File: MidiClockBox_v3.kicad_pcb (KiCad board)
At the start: 2 copper layers, 219 x 100 mm, 85 parts, among them J1 Midi In 0, J10 Display, J11 Midi Out 3, J12 Midi Out 4, J13 Midi Out 5, J14 Sync Out 0, J15 Sync Out 1, J16 Spare, J2 ICSP, J3 WS2812, J4 Conn_02x07_Odd_Even, J5 Conn_02x12_Counter_Clockwise, J6 Midi Out 0, J7 Midi Out 1, J8 Midi Out 2, J9 WS2812, SW1 RotaryEncoder_Switch, SW2 TAP, SW3 Start, SW4 Stop, SW5 Preset1, SW6 Preset2, SW7 Preset3, U1 CD74HC4067SM, U2 74LS241, U3 6N138, U4 74HC595, U6 74LS08, U7 74LS08, U8 74HC595, U9 74LS241

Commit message: add recent changes
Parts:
- added REF**: PinHeader_1x07_P2.54mm_Vertical, Connector_PinHeader_2.54mm:PinHeader_1x07_P2.54mm_Vertical, F.Cu at (164.4, 75.5)
- added REF**: PinHeader_1x07_P2.54mm_Vertical, Connector_PinHeader_2.54mm:PinHeader_1x07_P2.54mm_Vertical, F.Cu at (166.5, 83.5)
- moved J4 63.7 mm to (97.7, 116.5), turned to -90 degrees
- moved R15 56.8 mm to (127.0, 88.8), turned to -90 degrees
- moved C4 40.5 mm to (215.7, 64.8)
- moved U8 40.5 mm to (213.0, 71.5)
- moved C3 37.9 mm to (226.6, 53.6)
- moved U4 37.9 mm to (224.0, 60.0)
- moved R11 37.9 mm to (120.0, 88.8), turned to -90 degrees
- moved C2 31.6 mm to (202.6, 43.8)
- moved U2 31.6 mm to (206.0, 52.0)
- moved R9 31.0 mm to (116.0, 88.7), turned to -90 degrees
- moved J16 29.5 mm to (242.9, 74.5), turned to -90 degrees
- moved C7 27.0 mm to (242.6, 49.8), turned to 0 degrees
- moved R8 25.3 mm to (113.0, 88.7)
- moved R1 21.0 mm to (123.5, 88.7), turned to -90 degrees
- moved R7 19.7 mm to (110.0, 88.7)
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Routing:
- net IN_TAP: track 0.00 -> 265.2 mm, vias 0 -> 1
- net IN_START: track 0.00 -> 162.8 mm
- net SYNC_START_STOP_BUFFERED_0: track 0.00 -> 159.1 mm, vias 0 -> 4
- net SYNC_START_STOP_BUFFERED_1: track 0.00 -> 149.1 mm, vias 0 -> 4
- net DA1: track 0.00 -> 118.2 mm, vias 0 -> 4
- net MIDI_RX: track 0.00 -> 112.9 mm, vias 0 -> 4
- net DA0: track 0.00 -> 108.1 mm, vias 0 -> 2
- net IN_PRESET1: track 0.00 -> 107.2 mm
- net DA2: track 0.00 -> 104.5 mm, vias 0 -> 4
- net MIDI_TX: track 0.00 -> 102.8 mm, vias 0 -> 9
- net SYNC_TX_BUFFERED_1: track 0.00 -> 94.8 mm, vias 0 -> 6
- net IN_PRESET2: track 0.00 -> 92.9 mm
- net ENC_SW: track 0.00 -> 92.8 mm
- net SYNC_TX_BUFFERED_0: track 0.00 -> 91.8 mm, vias 0 -> 6
- net IN_15: track 0.00 -> 90.9 mm, vias 0 -> 2
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- added copper zone on B.Cu, net GND
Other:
- outline, holes or cut-outs redrawn
- board text removed: "Ports auf single board incl Arduino LED Stripe einzeln Buttons auf single board, wenig zuleitung, 2-seitig Panelize"

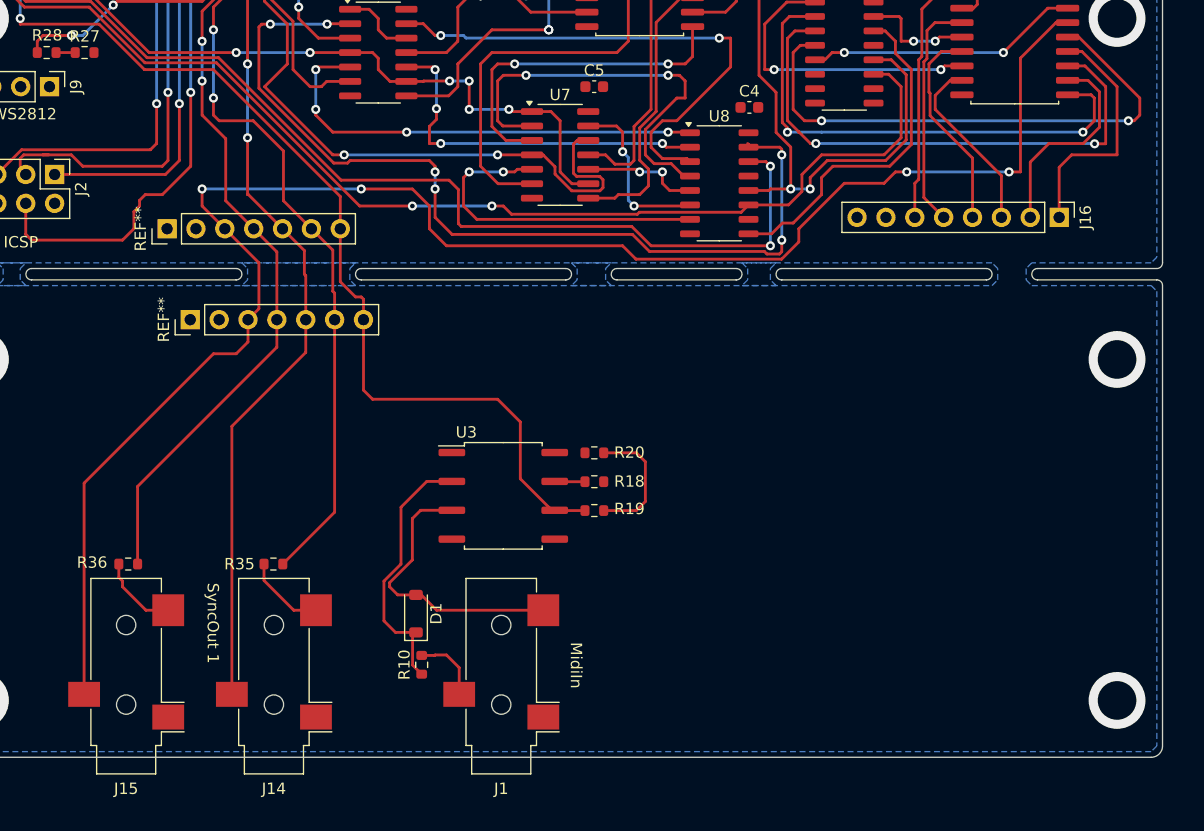
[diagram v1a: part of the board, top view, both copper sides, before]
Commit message: add breakout connectors for sync-out and midi-in
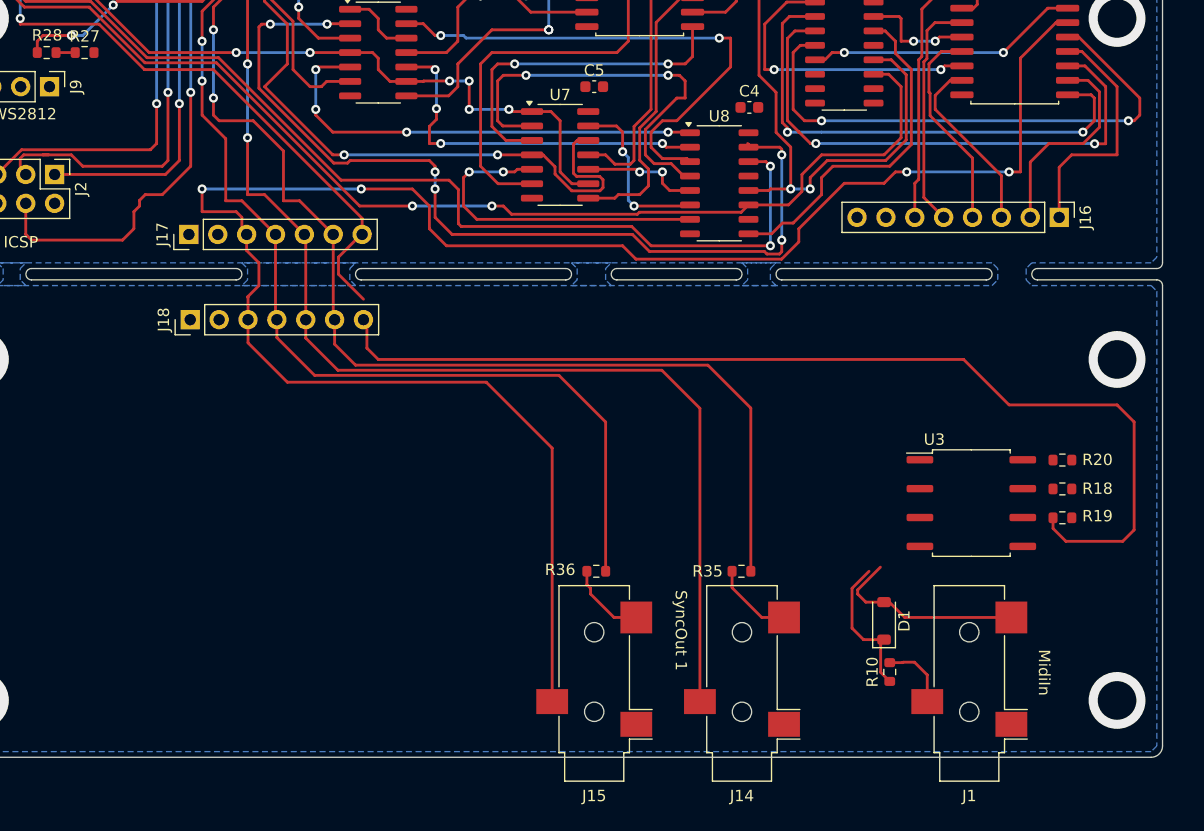
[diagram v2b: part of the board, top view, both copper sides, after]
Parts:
- removed REF** (x2): PinHeader_1x07_P2.54mm_Vertical, Connector_PinHeader_2.54mm:PinHeader_1x07_P2.54mm_Vertical
- added J17: Conn_01x07, Connector_PinHeader_2.54mm:PinHeader_1x07_P2.54mm_Vertical, F.Cu at (166.3, 76.0)
- added J18: Conn_01x07, Connector_PinHeader_2.54mm:PinHeader_1x07_P2.54mm_Vertical, F.Cu at (166.5, 83.5)
- moved D1 41.2 mm to (227.5, 110.0)
- moved J1 41.2 mm to (235.0, 115.5)
- moved J14 41.2 mm to (215.0, 115.5)
- moved J15 41.2 mm to (202.0, 115.5)
- moved R10 41.2 mm to (228.0, 114.5)
- moved R18 41.2 mm to (243.2, 98.4)
- moved R19 41.2 mm to (243.2, 100.9)
- moved R20 41.2 mm to (243.2, 95.9)
- moved R35 41.2 mm to (215.0, 105.6)
- moved R36 41.2 mm to (202.2, 105.6)
- moved U3 41.2 mm to (235.2, 99.6)
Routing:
- net MIDI_RX: track 112.9 -> 170.6 mm
- net SYNC_TX_BUFFERED_0: track 91.8 -> 124.7 mm
- net SYNC_START_STOP_BUFFERED_0: track 159.1 -> 188.9 mm
- net SYNC_TX_BUFFERED_1: track 94.8 -> 115.8 mm
- net SYNC_START_STOP_BUFFERED_1: track 149.1 -> 165.7 mm
- net Net-(R19-Pad2): track 11.5 -> 0.00 mm
- net Net-(D1-K): track 23.4 -> 13.0 mm
- net Net-(D1-A): track 25.0 -> 17.6 mm
- net Net-(U3-VO1): track 2.67 -> 0.00 mm

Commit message: pcb looks complete
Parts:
- added J19: Conn_02x05_Odd_Even, Connector_PinHeader_2.54mm:PinHeader_2x05_P2.54mm_Vertical, F.Cu at (155.2, 64.9)
- added J20: Conn_02x05_Odd_Even, Connector_PinHeader_2.54mm:PinHeader_2x05_P2.54mm_Vertical, F.Cu at (44.2, 64.9)
- moved J9 112.1 mm to (44.4, 39.5), turned to 90 degrees
- moved J2 98.3 mm to (246.5, 35.9), turned to 0 degrees
- moved R28 14.5 mm to (165.5, 68.7), turned to -90 degrees
- moved R27 9.90 mm to (165.5, 65.3), turned to 90 degrees
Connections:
- D2 pad 4: Net-(D2-DIN) -> LED_DATA
- J3 pad 2: Net-(D2-DIN) -> LED_DATA
- J5 pad 13: LED_DATA -> Net-(J5-Pin_13)
- J9 pad 2: Net-(J9-Pin_2) -> LED_DATA
- R27 pad 2: Net-(J9-Pin_2) -> Net-(J5-Pin_13)
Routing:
- net S0: track 0.08 -> 169.3 mm, vias 0 -> 8
- net S1: track 0.00 -> 166.7 mm, vias 0 -> 6
- net GND: track 0.00 -> 159.4 mm, vias 0 -> 57
- net SDA: track 0.00 -> 150.5 mm, vias 0 -> 4
- net DEMUX: track 0.00 -> 143.0 mm, vias 0 -> 6
- net +5V: track 0.00 -> 139.9 mm, vias 0 -> 44
- net S2: track 0.00 -> 137.8 mm, vias 0 -> 6
- net S3: track 0.00 -> 136.8 mm, vias 0 -> 6
- net SCL: track 0.00 -> 133.6 mm, vias 0 -> 4
- net MISO: track 36.9 -> 111.1 mm, vias 2 -> 4
- net SCLK: track 43.2 -> 112.3 mm
- net LED_DATA: track 21.4 -> 75.9 mm, vias 2 -> 0
- net MOSI: track 43.2 -> 85.8 mm
- net RST: track 56.7 -> 87.0 mm
- net IN_STOP: track 23.3 -> 40.4 mm, vias 0 -> 2
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- added copper zone on F.Cu, net +5V
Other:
- outline, holes or cut-outs redrawn
- board text removed: "ClockBox v3"
- board text removed: "Developed @BringTheNoise Hamburg"
- board text removed: "ICSP"
- board text removed: "Revision 202401001"
- board text removed: "www.Andyland.info"

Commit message: add silkscreen text
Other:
- board text added: "Andy Fischer Revision 202501001 info@Andyland.info info@SocialMidi.com"
- board text added: "ClockBox v3"
- board text added: "Encoder"
- board text added: "Midi IN"
- board text added: "Preset 1"
- board text added: "Preset 2"
- board text added: "Preset 3"
- board text added: "Spare 1"
- board text added: "Spare 2"
- board text added: "Start"
- board text added: "Stop"
- board text added: "Sync Out 0"
- board text added: "Sync Out 1"
- board text added: "TAP"
- board text removed: "MidiIn"
- board text removed: "SyncOut 0"
- board text removed: "SyncOut 1"
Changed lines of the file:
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@@
 		)
 		(property "Value" "Midi In 0"
-			(at -6.24 -7.41 90)
+			(at -6.24 -2.5 90)
 			(layer "F.Fab")
 			(effects
@@
 		)
 		(property "Value" "Sync Out 1"
-			(at -6.24 -6.14 90)
+			(at -6.5 -1.5 90)
 			(layer "F.Fab")
 			(effects
@@
 		)
 		(property "Value" "Sync Out 0"
-			(at -6.24 -6.14 90)
+			(at -6.5 -1.5 90)
 			(layer "F.Fab")
 			(effects
@@
 		)
 	)
+	(gr_text "TAP"
+		(at 63 50.5 90)
+		(layer "F.SilkS")
+		(effects
+			(font
+				(size 1 1)
+				(thickness 0.15)
+			)
+			(justify left bottom)
+		)
+	)
+	(gr_text "Start"
+		(at 50.5 107.5 90)
+		(layer "F.SilkS")
+		(effects
+			(font
+				(size 1 1)
+				(thickness 0.15)
+			)
+			(justify left bottom)
+		)
+	)
 	(gr_text "MidiOut 4"
 		(at 175.012 39.178 90)
@@
 		)
 	)
-	(gr_text "SyncOut 0"
-		(at 243.592 38.67 90)
+	(gr_text "Preset 1"
+		(at 75.5 108 90)
 		(layer "F.SilkS")
 		(effects
@@
 		)
 	)
-	(gr_text "MidiIn"
-		(at 241 112.5 -90)
+	(gr_text "Andy Fischer\nRevision 202501001\n\ninfo@Andyland.info\ninfo@SocialMidi.com"
+		(at 150.5 105.5 0)
+		(layer "F.SilkS")
+		(effects
+			(font
+				(size 1 1)
+				(thickness 0.15)
+			)
+			(justify left bottom)
+		)
+	)
+	(gr_text "WS2812"
+		(at 51.5 40 0)
+		(layer "F.SilkS")
+		(effects
+			(font
+				(size 1 1)
+				(thickness 0.15)
+			)
+			(justify left bottom)
+		)
+	)
+	(gr_text "Stop"
+		(at 140.5 108 90)
+		(layer "F.SilkS")
+		(effects
+			(font
+				(size 1 1)
+				(thickness 0.15)
+			)
+			(justify left bottom)
+		)
+	)
+	(gr_text "Encoder"
+		(at 129 50 90)
+		(layer "F.SilkS")
+		(effects
+			(font
+				(size 1 1)
+				(thickness 0.15)
+			)
+			(justify left bottom)
+		)
+	)
+	(gr_text "Spare 1"
+		(at 74 117.5 0)
+		(layer "F.SilkS")
+		(effects
+			(font
+				(size 1 1)
+				(thickness 0.15)
+			)
+			(justify left bottom)
+		)
+	)
+	(gr_text "Midi IN"
+		(at 240.5 117 90)
 		(layer "F.SilkS")
 		(effects
@@
 		)
 	)
+	(gr_text "Preset 3"
+		(at 115.5 108 90)
+		(layer "F.SilkS")
+		(effects
+			(font
+				(size 1 1)
+				(thickness 0.15)
+			)
+			(justify left bottom)
+		)
+	)
 	(gr_text "MidiOut 2"
 		(at 209.429 39.051 90)
@@
 		)
 	)
-	(gr_text "Display"
-		(at 80 45 0)
+	(gr_text "Spare 2"
+		(at 224 77.5 0)
+		(layer "F.SilkS")
+		(effects
+			(font
+				(size 1 1)
+				(thickness 0.15)
+			)
+			(justify left bottom)
+		)
+	)
+	(gr_text "ClockBox v3"
+		(at 150 97.5 0)
+		(layer "F.SilkS")
+		(effects
+			(font
+				(size 3 3)
+				(thickness 0.45)
+			)
+			(justify left bottom)
+		)
+	)
+	(gr_text "Sync Out 0"
+		(at 211 115 90)
 		(layer "F.SilkS")
 		(effects
@@
 		)
 	)
-	(gr_text "SyncOut 1"
-		(at 209.048 107.287 -90)
+	(gr_text "Preset 2"
+		(at 95.5 108 90)
+		(layer "F.SilkS")
+		(effects
+			(font
+				(size 1 1)
+				(thickness 0.15)
+			)
+			(justify left bottom)
+		)
+	)
+	(gr_text "Display"
+		(at 80 45 0)
 		(layer "F.SilkS")
 		(effects
@@
 		)
 	)
+	(gr_text "Sync Out 1"
+		(at 198 115 90)
+		(layer "F.SilkS")
+		(effects
+			(font
+				(size 1 1)
+				(thickness 0.15)
+			)
+			(justify left bottom)
+		)
+	)
 	(gr_text "MidiOut 1"
 		(at 220.986 38.924 90)
@@
 	)
 	(group ""
-		(members "61c501ca-7f42-4c20-99ac-3da20b899098" "a9465e44-3ca1-40e0-b603-d75388b29636"
-			"bc7c0856-c1d8-49b7-a063-d90ff8a64daf" "bfdfbc6c-9df6-4fc4-8a9f-e6215f7882e6"
-			"dcbcfb31-942c-4bba-b492-3723081075cb"
-		)
-	)
-	(group ""
-		(members "0d29409a-70a7-470f-a961-6b71b25106f6" "29d8489d-5353-475b-a9cf-e43c7dab7fae"
-			"30d6202a-4769-4309-ae90-fce66a4c40b3" "3292afcf-8b89-49b0-bf3b-336a607fef0b"
-			"337340bd-9962-411b-9636-54bbb4d318a6" "4777c9db-d456-4fd3-83cb-861a80502c02"
-			"4c74b6d2-6ab8-4eb1-9cb1-cdd85d8c6bf9" "57771380-6904-4cfb-9b5e-e0dcae7f8e5e"
-			"6a0df784-f801-4e2e-8e16-45414ec7c5cd" "70152826-7a5e-4838-bf02-0dd82f9033eb"
-			"71fdc79e-6370-407f-a44a-43016a0e27bc" "7ddab6a4-52ee-4c61-b293-b4eb6bcab8b5"
-			"84dc04c1-4c93-484e-8a26-e8f5b8868460" "882612e0-db30-4401-95d3-3f485178e6e2"
-			"90eafc24-c84f-45e5-8213-36297800184f" "91ffd533-0382-4dc8-b368-83a1d50c28b2"
-			"925ee635-54b8-4d4d-bb15-e7f3d29ce3c4" "99de6df6-4cf4-4b61-8710-9346c931a96c"
-			"ac4091c6-4054-4bcf-8aee-a0710218f526" "d476e249-f8d0-415d-9ace-e43d327e42e4"
-			"d6680d1b-f713-480f-a815-3d1043845107" "e64f28f9-baeb-4cf2-9f05-a0ceaeee8b88"
-			"e9037d01-5435-4f8e-8f63-2f8f428bb70a" "eac952d6-dbb9-4beb-8a0a-9d37bc132b20"
-			"f485458b-d93f-40af-bafa-a373df841667"
-		)
+		(members "3a8089f8-211b-4fdb-ac50-9c72ace80fbe" "adf44df8-b698-4b34-9b0c-c6378024180b")
 	)
 )

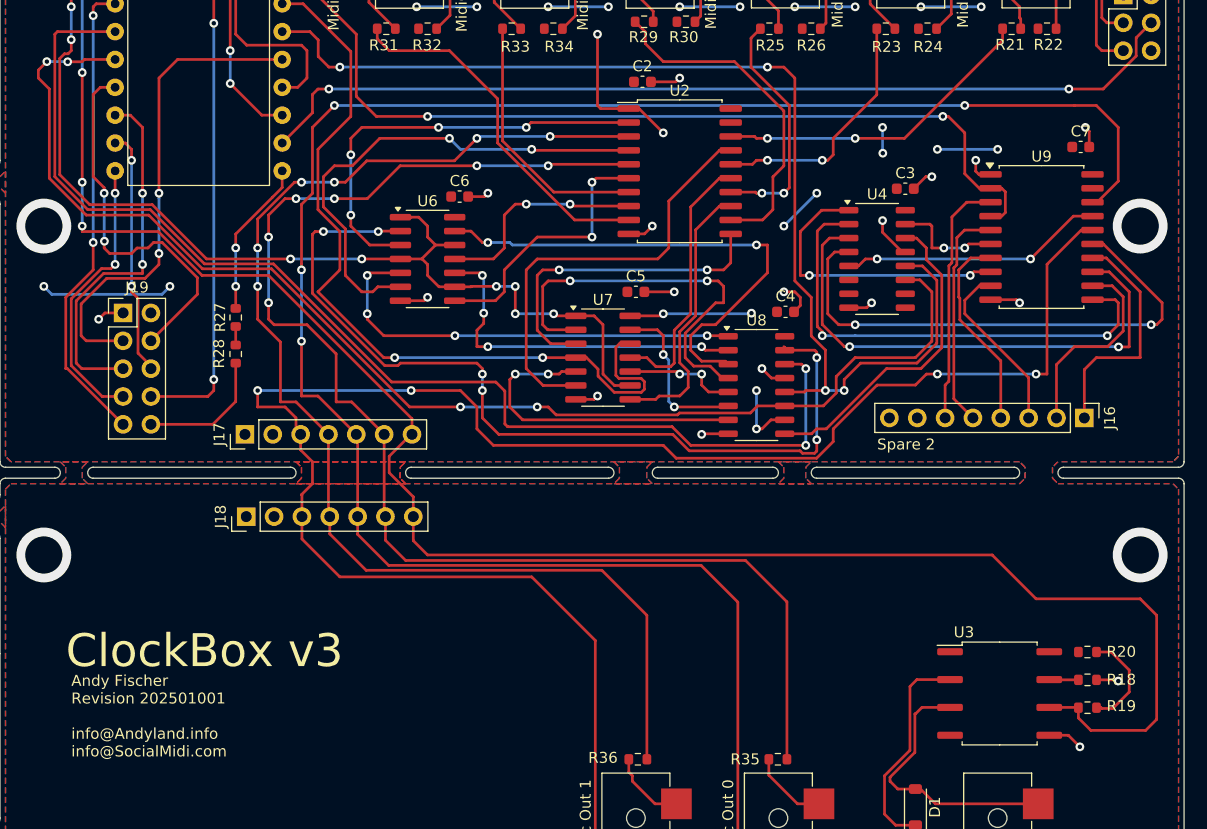
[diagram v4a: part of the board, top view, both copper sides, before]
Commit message: add silkscreen text
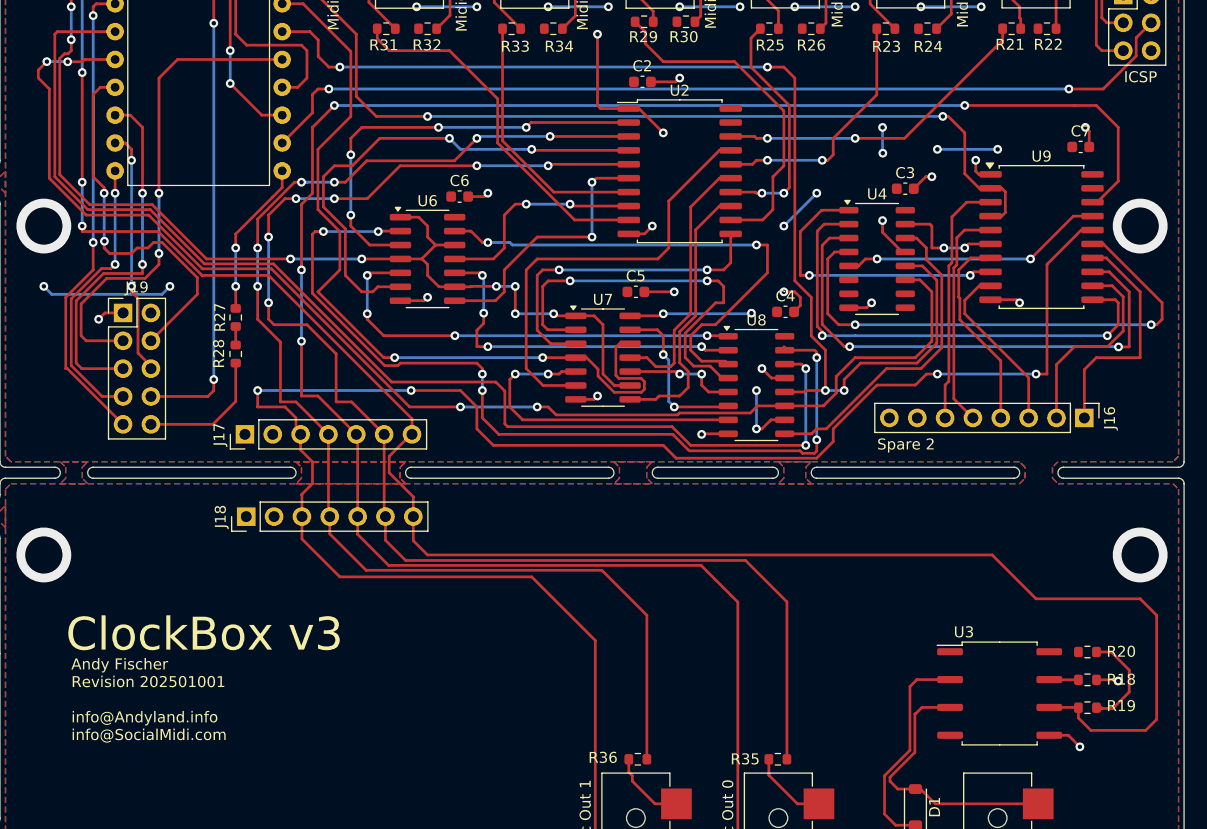
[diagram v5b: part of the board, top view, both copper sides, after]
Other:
- board text added: "ICSP"
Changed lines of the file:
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@@
 	)
 	(gr_text "Andy Fischer\nRevision 202501001\n\ninfo@Andyland.info\ninfo@SocialMidi.com"
-		(at 150.5 105.5 0)
+		(at 150.5 104 0)
 		(layer "F.SilkS")
 		(effects
@@
 	)
 	(gr_text "ClockBox v3"
-		(at 150 97.5 0)
+		(at 150 96 0)
 		(layer "F.SilkS")
 		(effects
@@
 		(layer "F.SilkS")
 		(effects
+			(font
+				(size 1 1)
+				(thickness 0.15)
+			)
+			(justify left bottom)
+		)
+	)
+	(gr_text "ICSP"
+		(at 246.5 44 0)
+		(layer "F.SilkS")
+		(effects
